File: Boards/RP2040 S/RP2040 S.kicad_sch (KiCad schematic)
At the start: 2 parts, among them J1 Conn_01x20_Pin, J3 Conn_01x18_Pin

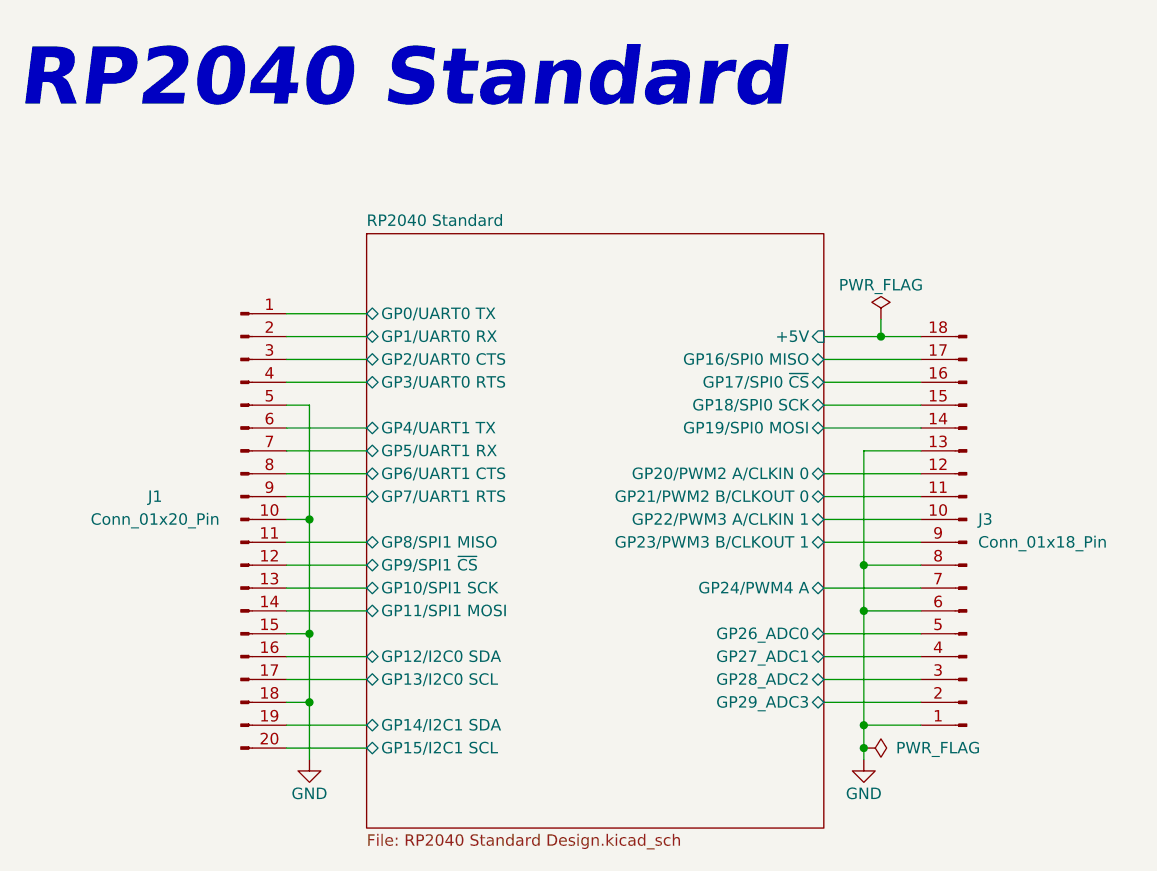
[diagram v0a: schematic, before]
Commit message: Sockets Pico_Conn
Adição à Library e ao RP2040 S de Sockets iguais às placas de Pico.
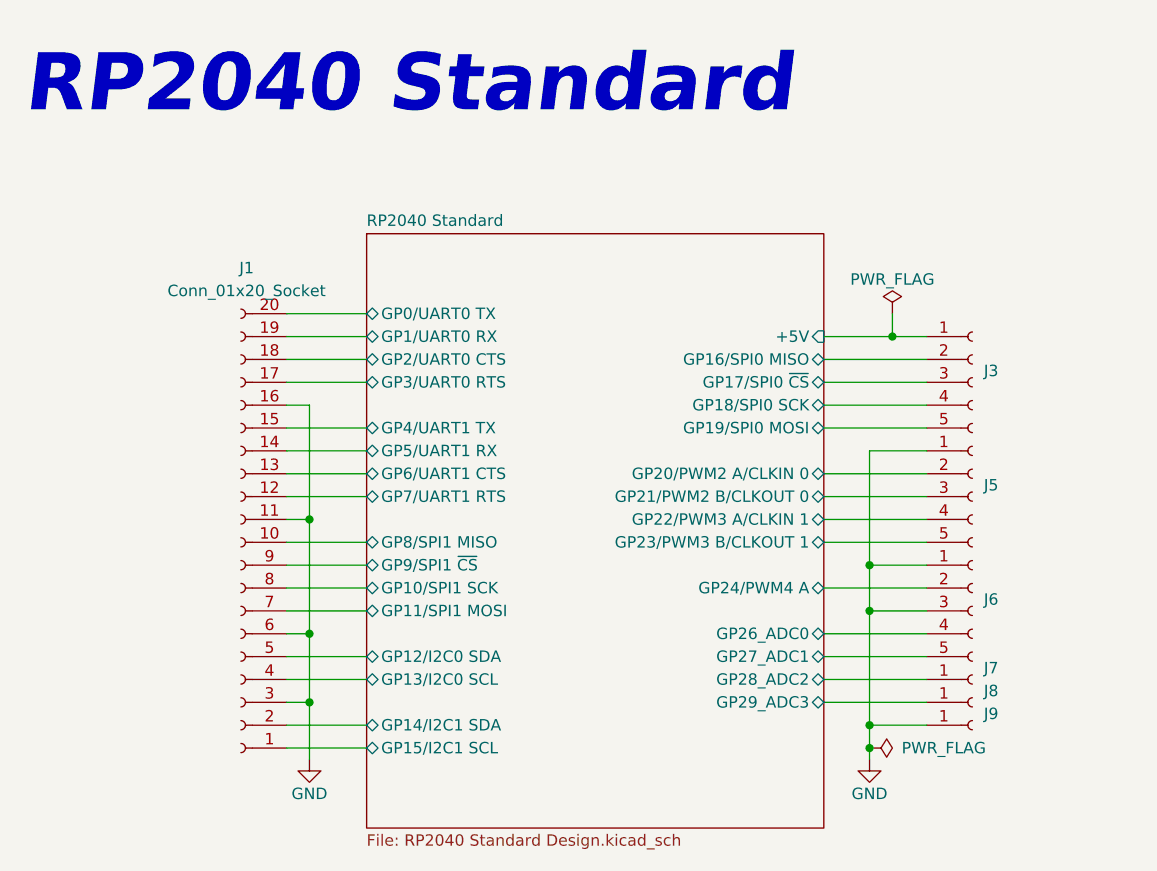
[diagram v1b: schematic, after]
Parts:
- removed J1: Conn_01x20_Pin, symbol Connector:Conn_01x20_Pin
- removed J3: Conn_01x18_Pin, symbol Connector:Conn_01x18_Pin
- added J1: Conn_01x20_Socket, Pico_Conn1x20:Pico_20pin, symbol Connector:Conn_01x20_Socket
- added J3, J5, J6: Conn_01x05_Socket, Pico_Conn1x5:Pico_05pin, symbol Connector:Conn_01x05_Socket
- added J7, J8, J9: Conn_01x01_Socket, Pico_Conn1x1:Pico_01pin, symbol Connector:Conn_01x01_Socket
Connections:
- net GND: now also J1.11 (Pin_11), J1.16 (Pin_16), J1.3 (Pin_3), J1.6 (Pin_6), J5.1 (Pin_1), J6.1 (Pin_1), J6.3 (Pin_3), J9.1 (Pin_1)
- net RP2040 Standard/+5V: now also J3.1 (Pin_1)
- net RP2040 Standard/GP0/UART0 TX: now also J1.20 (Pin_20)
- net RP2040 Standard/GP10/SPI1 SCK: now also J1.8 (Pin_8)
- net RP2040 Standard/GP11/SPI1 MOSI: now also J1.7 (Pin_7)
- net RP2040 Standard/GP12/I2C0 SDA: now also J1.5 (Pin_5)
- net RP2040 Standard/GP13/I2C0 SCL: now also J1.4 (Pin_4)
- net RP2040 Standard/GP14/I2C1 SDA: now also J1.2 (Pin_2)
- net RP2040 Standard/GP15/I2C1 SCL: now also J1.1 (Pin_1)
- net RP2040 Standard/GP16/SPI0 MISO: now also J3.2 (Pin_2)
- net RP2040 Standard/GP17/SPI0 ~{CS}: now also J3.3 (Pin_3)
- net RP2040 Standard/GP18/SPI0 SCK: now also J3.4 (Pin_4)
- net RP2040 Standard/GP19/SPI0 MOSI: now also J3.5 (Pin_5)
- net RP2040 Standard/GP1/UART0 RX: now also J1.19 (Pin_19)
- net RP2040 Standard/GP20/PWM2 A/CLKIN 0: now also J5.2 (Pin_2)
- net RP2040 Standard/GP21/PWM2 B/CLKOUT 0: now also J5.3 (Pin_3)
- net RP2040 Standard/GP22/PWM3 A/CLKIN 1: now also J5.4 (Pin_4)
- net RP2040 Standard/GP23/PWM3 B/CLKOUT 1: now also J5.5 (Pin_5)
- net RP2040 Standard/GP24/PWM4 A: now also J6.2 (Pin_2)
- net RP2040 Standard/GP26_ADC0: now also J6.4 (Pin_4)
- net RP2040 Standard/GP27_ADC1: now also J6.5 (Pin_5)
- net RP2040 Standard/GP28_ADC2: now also J7.1 (Pin_1)
- net RP2040 Standard/GP29_ADC3: now also J8.1 (Pin_1)
- net RP2040 Standard/GP2/UART0 CTS: now also J1.18 (Pin_18)
- net RP2040 Standard/GP3/UART0 RTS: now also J1.17 (Pin_17)
- net RP2040 Standard/GP4/UART1 TX: now also J1.15 (Pin_15)
- net RP2040 Standard/GP5/UART1 RX: now also J1.14 (Pin_14)
- net RP2040 Standard/GP6/UART1 CTS: now also J1.13 (Pin_13)
- net RP2040 Standard/GP7/UART1 RTS: now also J1.12 (Pin_12)
- net RP2040 Standard/GP8/SPI1 MISO: now also J1.10 (Pin_10)
- net RP2040 Standard/GP9/SPI1 ~{CS}: now also J1.9 (Pin_9)
